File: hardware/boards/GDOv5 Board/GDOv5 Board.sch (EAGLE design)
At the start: 29 parts, among them IC1 DS1820, IC2 3.3V REG, J1 DCJ0202

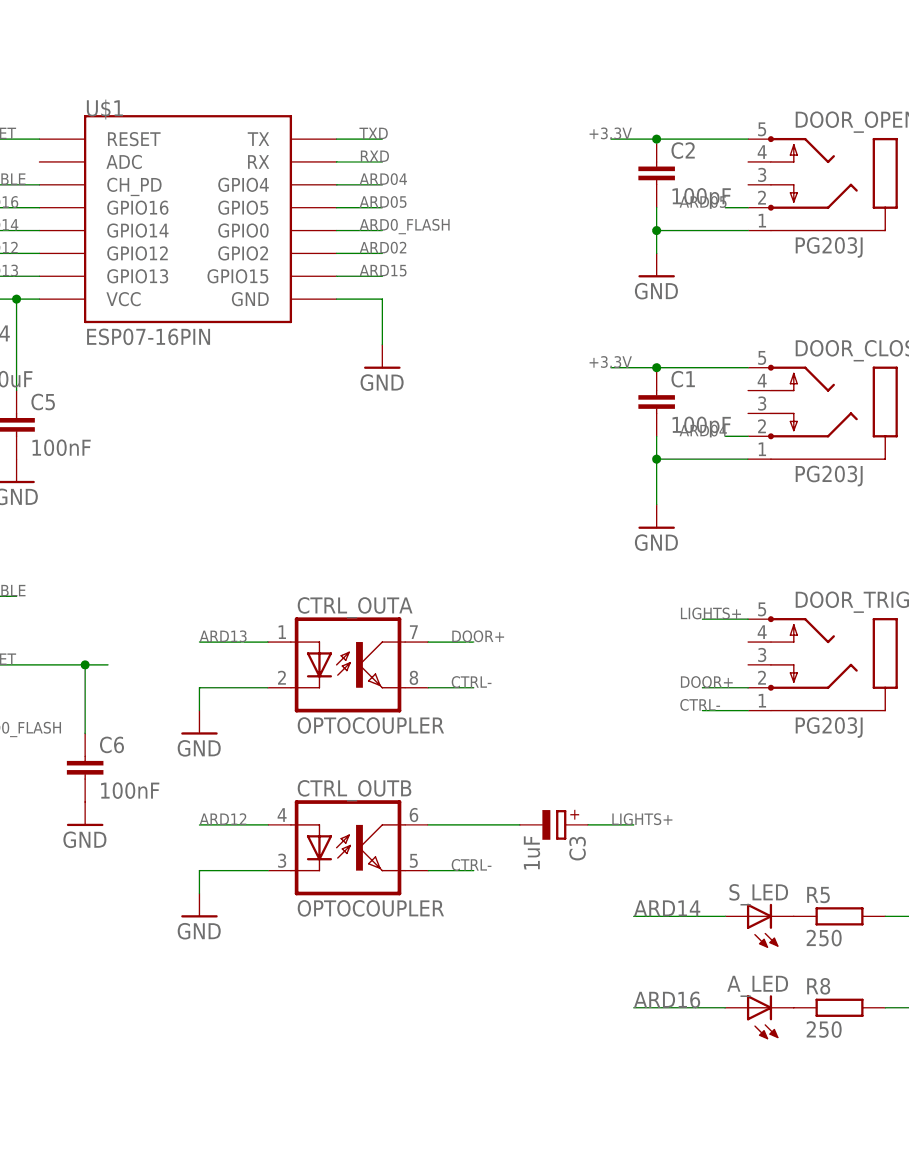
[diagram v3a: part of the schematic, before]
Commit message: Added resistor for optocoupler inputs
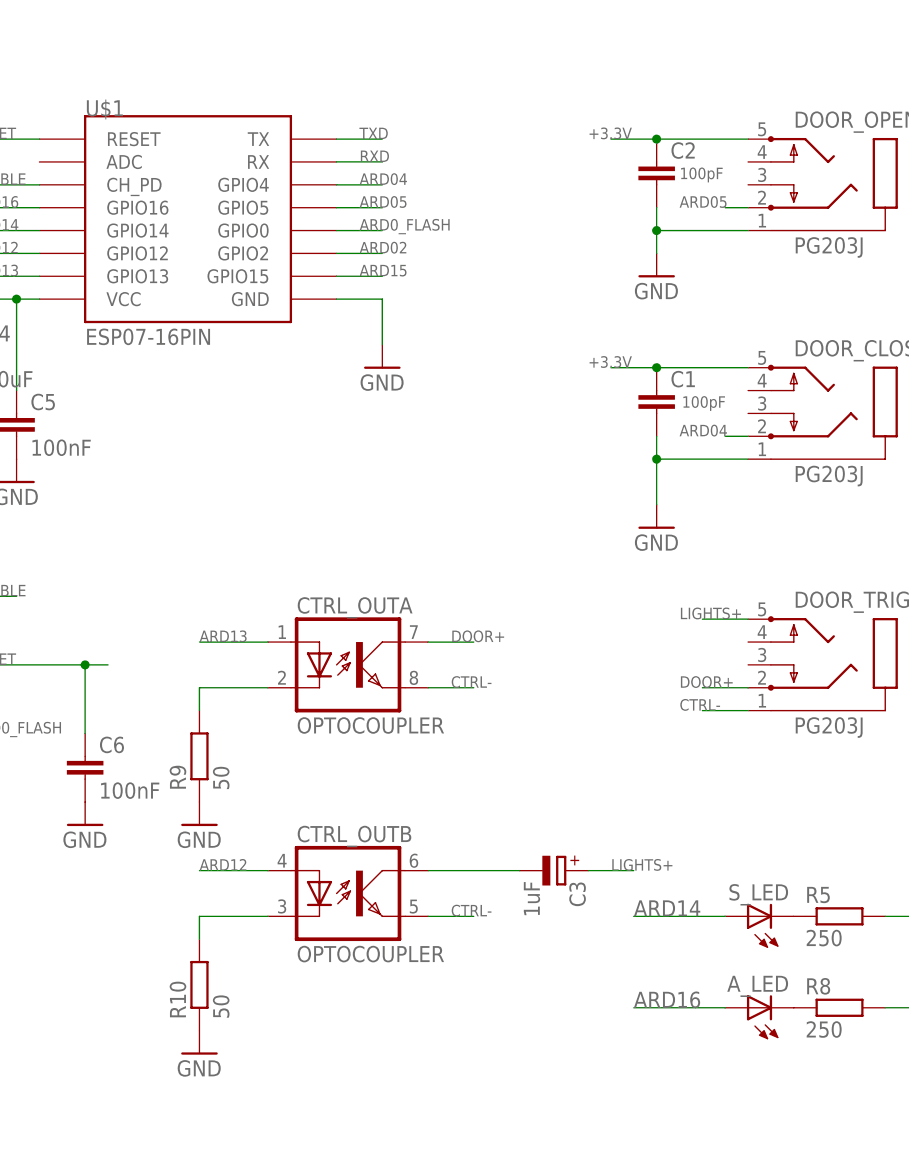
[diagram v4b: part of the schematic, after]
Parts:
- added R10, R9: 50, resistor:R-EU_M3216
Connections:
- new net N$6: CTRL_OUTA.C, R9.2
- new net N$7: CTRL_OUTB.C, R10.2
- net GND: now also R10.1, R9.1; no longer CTRL_OUTA.C, CTRL_OUTB.C
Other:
- moved on the sheet: C3, CTRL_OUTB
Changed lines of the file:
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@@
 <?xml version="1.0" encoding="utf-8"?>
 <!DOCTYPE eagle SYSTEM "eagle.dtd">
-<eagle version="7.5.0">
+<eagle version="7.4.0">
 <drawing>
 <settings>
@@
 <part name="C2" library="resistor" deviceset="C-EU" device="C1206" value="100pF"/>
 <part name="C3" library="rcl" deviceset="CPOL-EU" device="CT3216" value="1uF"/>
-<part name="GND5" library="supply1" deviceset="GND" device=""/>
-<part name="GND6" library="supply1" deviceset="GND" device=""/>
 <part name="GND7" library="supply1" deviceset="GND" device=""/>
 <part name="R1" library="resistor" deviceset="R-EU_" device="M3216" value="4.7K"/>
@@
 <part name="GND10" library="supply1" deviceset="GND" device=""/>
 <part name="GND12" library="supply1" deviceset="GND" device=""/>
+<part name="R9" library="resistor" deviceset="R-EU_" device="M3216" value="50"/>
+<part name="GND5" library="supply1" deviceset="GND" device=""/>
+<part name="R10" library="resistor" deviceset="R-EU_" device="M3216" value="50"/>
+<part name="GND13" library="supply1" deviceset="GND" device=""/>
 </parts>
 <sheets>
@@
 <instance part="J1" gate="G$1" x="-12.7" y="111.76"/>
 <instance part="CTRL_OUT" gate="A" x="93.98" y="40.64"/>
-<instance part="CTRL_OUT" gate="B" x="93.98" y="20.32"/>
+<instance part="CTRL_OUT" gate="B" x="93.98" y="15.24"/>
 <instance part="IC1" gate="G$1" x="-2.54" y="83.82"/>
 <instance part="IC2" gate="G$1" x="-5.08" y="53.34"/>
@@
 <instance part="GND3" gate="1" x="127" y="55.88"/>
 <instance part="GND4" gate="1" x="127" y="83.82"/>
-<instance part="C1" gate="G$1" x="127" y="71.12"/>
-<instance part="C2" gate="G$1" x="127" y="96.52"/>
-<instance part="C3" gate="G$1" x="116.84" y="22.86" rot="R270"/>
-<instance part="GND5" gate="1" x="76.2" y="33.02"/>
-<instance part="GND6" gate="1" x="76.2" y="12.7"/>
+<instance part="C1" gate="G$1" x="127" y="71.12" smashed="yes">
+<attribute name="NAME" x="128.524" y="71.501" size="1.778" layer="95"/>
+<attribute name="VALUE" x="129.794" y="69.215" size="1.27" layer="96"/>
+</instance>
+<instance part="C2" gate="G$1" x="127" y="96.52" smashed="yes">
+<attribute name="NAME" x="128.524" y="96.901" size="1.778" layer="95"/>
+<attribute name="VALUE" x="129.54" y="94.615" size="1.27" layer="96"/>
+</instance>
+<instance part="C3" gate="G$1" x="116.84" y="17.78" rot="R270"/>
 <instance part="GND7" gate="1" x="96.52" y="73.66"/>
 <instance part="R1" gate="G$1" x="-2.54" y="93.98"/>
@@
 <instance part="GND10" gate="1" x="157.48" y="-7.62"/>
 <instance part="GND12" gate="1" x="-2.54" y="71.12"/>
+<instance part="R9" gate="G$1" x="76.2" y="30.48" rot="R90"/>
+<instance part="GND5" gate="1" x="76.2" y="22.86"/>
+<instance part="R10" gate="G$1" x="76.2" y="5.08" rot="R90"/>
+<instance part="GND13" gate="1" x="76.2" y="-2.54"/>
 </instances>
 <busses>
@@
 </segment>
 <segment>
-<pinref part="CTRL_OUT" gate="A" pin="C"/>
-<wire x1="83.82" y1="38.1" x2="76.2" y2="38.1" width="0.1524" layer="91"/>
-<wire x1="76.2" y1="38.1" x2="76.2" y2="35.56" width="0.1524" layer="91"/>
-<pinref part="GND5" gate="1" pin="GND"/>
-</segment>
-<segment>
-<pinref part="CTRL_OUT" gate="B" pin="C"/>
-<wire x1="83.82" y1="17.78" x2="76.2" y2="17.78" width="0.1524" layer="91"/>
-<wire x1="76.2" y1="17.78" x2="76.2" y2="15.24" width="0.1524" layer="91"/>
-<pinref part="GND6" gate="1" pin="GND"/>
-</segment>
-<segment>
 <pinref part="U$1" gate="G$1" pin="GND"/>
 <wire x1="91.44" y1="81.28" x2="96.52" y2="81.28" width="0.1524" layer="91"/>
@@
 <wire x1="-2.54" y1="73.66" x2="-2.54" y2="71.12" width="0.1524" layer="91"/>
 <junction x="-2.54" y="73.66"/>
+</segment>
+<segment>
+<pinref part="R9" gate="G$1" pin="1"/>
+<pinref part="GND5" gate="1" pin="GND"/>
+</segment>
+<segment>
+<pinref part="R10" gate="G$1" pin="1"/>
+<pinref part="GND13" gate="1" pin="GND"/>
 </segment>
 </net>
@@
 <segment>
 <pinref part="CTRL_OUT" gate="B" pin="EMIT"/>
-<wire x1="101.6" y1="17.78" x2="106.68" y2="17.78" width="0.1524" layer="91"/>
-<label x="104.14" y="17.78" size="1.27" layer="95"/>
+<wire x1="101.6" y1="12.7" x2="106.68" y2="12.7" width="0.1524" layer="91"/>
+<label x="104.14" y="12.7" size="1.27" layer="95"/>
 </segment>
 <segment>
@@
 <segment>
 <pinref part="CTRL_OUT" gate="B" pin="COL"/>
-<wire x1="101.6" y1="22.86" x2="111.76" y2="22.86" width="0.1524" layer="91"/>
+<wire x1="101.6" y1="17.78" x2="111.76" y2="17.78" width="0.1524" layer="91"/>
 <pinref part="C3" gate="G$1" pin="-"/>
 </segment>
@@
 <segment>
 <pinref part="C3" gate="G$1" pin="+"/>
-<wire x1="119.38" y1="22.86" x2="124.46" y2="22.86" width="0.1524" layer="91"/>
-<label x="121.92" y="22.86" size="1.27" layer="95"/>
+<wire x1="119.38" y1="17.78" x2="124.46" y2="17.78" width="0.1524" layer="91"/>
+<label x="121.92" y="17.78" size="1.27" layer="95"/>
 </segment>
 <segment>
@@
 <segment>
 <pinref part="CTRL_OUT" gate="B" pin="A"/>
-<wire x1="83.82" y1="22.86" x2="76.2" y2="22.86" width="0.1524" layer="91"/>
-<label x="76.2" y="22.86" size="1.27" layer="95"/>
+<wire x1="83.82" y1="17.78" x2="76.2" y2="17.78" width="0.1524" layer="91"/>
+<label x="76.2" y="17.78" size="1.27" layer="95"/>
 </segment>
 <segment>
@@
 </segment>
 </net>
+<net name="N$6" class="0">
+<segment>
+<pinref part="CTRL_OUT" gate="A" pin="C"/>
+<wire x1="83.82" y1="38.1" x2="76.2" y2="38.1" width="0.1524" layer="91"/>
+<wire x1="76.2" y1="38.1" x2="76.2" y2="35.56" width="0.1524" layer="91"/>
+<pinref part="R9" gate="G$1" pin="2"/>
+</segment>
+</net>
+<net name="N$7" class="0">
+<segment>
+<pinref part="CTRL_OUT" gate="B" pin="C"/>
+<wire x1="83.82" y1="12.7" x2="76.2" y2="12.7" width="0.1524" layer="91"/>
+<wire x1="76.2" y1="12.7" x2="76.2" y2="10.16" width="0.1524" layer="91"/>
+<pinref part="R10" gate="G$1" pin="2"/>
+</segment>
+</net>

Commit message: More board tweaks
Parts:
- removed C5: 100nF, resistor:C-EUC1206
- added C8, C9: 10uF, SparkFun-Capacitors:10UF-TANT
- C3: device rcl:CPOL-EUCT3216 -> SparkFun-Capacitors:CAP1206
- C4: value 10uF -> 100nF
- D1, D2, D3: device diode:SCHOTTKY-DIODESMD -> adafruit:DIODESOD-123
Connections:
- net +3.3V: now also C9.+; no longer C5.1
- net +5V: now also C8.+
- net GND: now also C8.-, C9.-; no longer C5.2
- net LIGHTS+: now also C3.2; no longer C3.+
- net N$3: now also C3.1; no longer C3.-
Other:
- moved on the sheet: C4

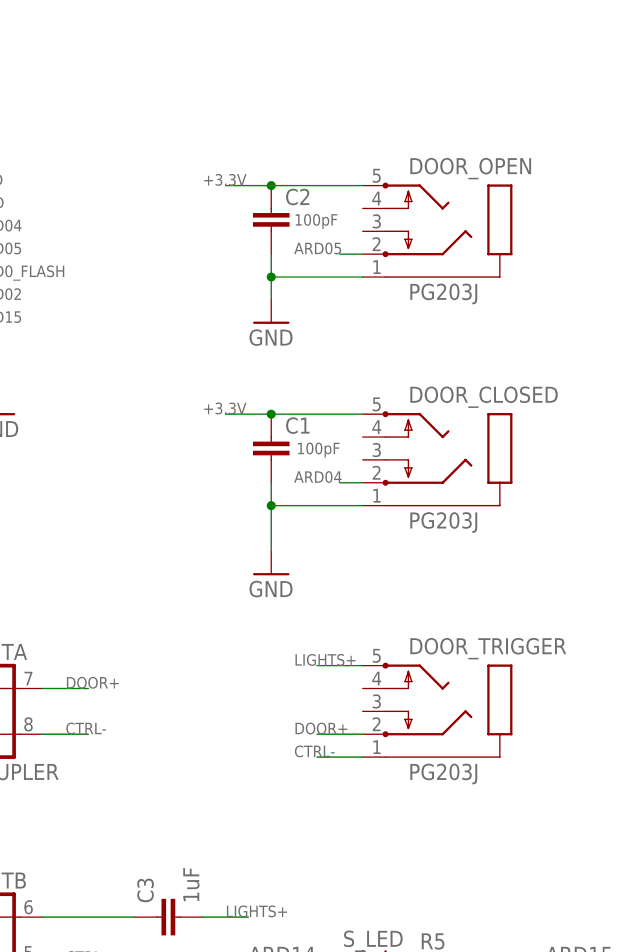
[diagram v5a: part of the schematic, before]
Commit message: Replacing 3.5mm Jack with SMT design
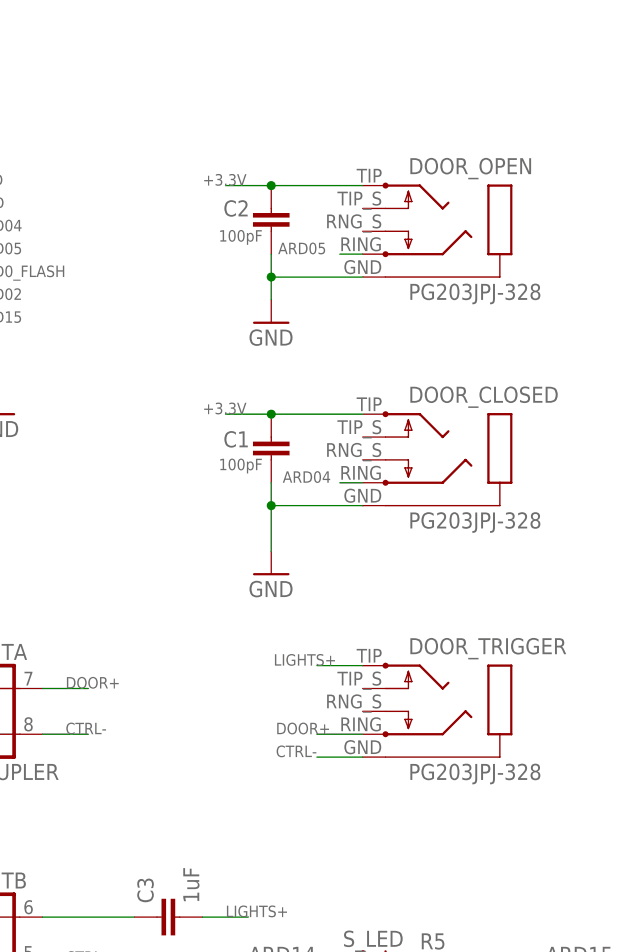
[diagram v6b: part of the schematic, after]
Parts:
- DOOR_CLOSED, DOOR_OPEN, DOOR_TRIGGER: value PG203J -> PG203JPJ-328; device con-hirschmann:PG203J -> PJ-328 Jack:PG203JPJ-328
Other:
- moved on the sheet: DOOR_CLOSED, DOOR_OPEN, DOOR_TRIGGER
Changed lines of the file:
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@@
 <grid distance="0.1" unitdist="inch" unit="inch" style="lines" multiple="1" display="no" altdistance="0.01" altunitdist="inch" altunit="inch"/>
 <layers>
-<layer number="1" name="Top" color="4" fill="1" visible="yes" active="no"/>
-<layer number="16" name="Bottom" color="1" fill="1" visible="yes" active="no"/>
-<layer number="17" name="Pads" color="2" fill="1" visible="yes" active="no"/>
-<layer number="18" name="Vias" color="2" fill="1" visible="yes" active="no"/>
-<layer number="19" name="Unrouted" color="6" fill="1" visible="yes" active="no"/>
-<layer number="20" name="Dimension" color="15" fill="1" visible="yes" active="no"/>
-<layer number="21" name="tPlace" color="7" fill="1" visible="yes" active="no"/>
-<layer number="22" name="bPlace" color="7" fill="1" visible="yes" active="no"/>
-<layer number="23" name="tOrigins" color="15" fill="1" visible="yes" active="no"/>
-<layer number="24" name="bOrigins" color="15" fill="1" visible="yes" active="no"/>
-<layer number="25" name="tNames" color="7" fill="1" visible="yes" active="no"/>
-<layer number="26" name="bNames" color="7" fill="1" visible="yes" active="no"/>
-<layer number="27" name="tValues" color="7" fill="1" visible="yes" active="no"/>
-<layer number="28" name="bValues" color="7" fill="1" visible="yes" active="no"/>
+<layer number="1" name="Top" color="4" fill="1" visible="no" active="no"/>
+<layer number="16" name="Bottom" color="1" fill="1" visible="no" active="no"/>
+<layer number="17" name="Pads" color="2" fill="1" visible="no" active="no"/>
+<layer number="18" name="Vias" color="2" fill="1" visible="no" active="no"/>
+<layer number="19" name="Unrouted" color="6" fill="1" visible="no" active="no"/>
+<layer number="20" name="Dimension" color="15" fill="1" visible="no" active="no"/>
+<layer number="21" name="tPlace" color="7" fill="1" visible="no" active="no"/>
+<layer number="22" name="bPlace" color="7" fill="1" visible="no" active="no"/>
+<layer number="23" name="tOrigins" color="15" fill="1" visible="no" active="no"/>
+<layer number="24" name="bOrigins" color="15" fill="1" visible="no" active="no"/>
+<layer number="25" name="tNames" color="7" fill="1" visible="no" active="no"/>
+<layer number="26" name="bNames" color="7" fill="1" visible="no" active="no"/>
+<layer number="27" name="tValues" color="7" fill="1" visible="no" active="no"/>
+<layer number="28" name="bValues" color="7" fill="1" visible="no" active="no"/>
 <layer number="29" name="tStop" color="7" fill="3" visible="no" active="no"/>
 <layer number="30" name="bStop" color="7" fill="6" visible="no" active="no"/>
@@
 <layer number="35" name="tGlue" color="7" fill="4" visible="no" active="no"/>
 <layer number="36" name="bGlue" color="7" fill="5" visible="no" active="no"/>
-<layer number="37" name="tTest" color="7" fill="1" visible="yes" active="no"/>
-<layer number="38" name="bTest" color="7" fill="1" visible="yes" active="no"/>
+<layer number="37" name="tTest" color="7" fill="1" visible="no" active="no"/>
+<layer number="38" name="bTest" color="7" fill="1" visible="no" active="no"/>
 <layer number="39" name="tKeepout" color="4" fill="11" visible="no" active="no"/>
 <layer number="40" name="bKeepout" color="1" fill="11" visible="no" active="no"/>
@@
 <layer number="44" name="Drills" color="7" fill="1" visible="no" active="no"/>
 <layer number="45" name="Holes" color="7" fill="1" visible="no" active="no"/>
-<layer number="46" name="Milling" color="3" fill="1" visible="yes" active="no"/>
-<layer number="47" name="Measures" color="7" fill="1" visible="yes" active="no"/>
-<layer number="48" name="Document" color="7" fill="1" visible="yes" active="no"/>
-<layer number="49" name="Reference" color="7" fill="1" visible="yes" active="no"/>
-<layer number="50" name="dxf" color="7" fill="1" visible="yes" active="no"/>
-<layer number="51" name="tDocu" color="7" fill="1" visible="yes" active="no"/>
-<layer number="52" name="bDocu" color="7" fill="1" visible="yes" active="no"/>
-<layer number="53" name="tGND_GNDA" color="7" fill="9" visible="yes" active="no"/>
-<layer number="54" name="bGND_GNDA" color="1" fill="9" visible="yes" active="no"/>
-<layer number="56" name="wert" color="7" fill="1" visible="yes" active="no"/>
-<layer number="57" name="tCAD" color="7" fill="1" visible="yes" active="no"/>
-<layer number="59" name="tCarbon" color="7" fill="1" visible="yes" active="no"/>
-<layer number="60" name="bCarbon" color="7" fill="1" visible="yes" active="no"/>
+<layer number="46" name="Milling" color="3" fill="1" visible="no" active="no"/>
+<layer number="47" name="Measures" color="7" fill="1" visible="no" active="no"/>
+<layer number="48" name="Document" color="7" fill="1" visible="no" active="no"/>
+<layer number="49" name="Reference" color="7" fill="1" visible="no" active="no"/>
+<layer number="50" name="dxf" color="7" fill="1" visible="no" active="no"/>
+<layer number="51" name="tDocu" color="7" fill="1" visible="no" active="no"/>
+<layer number="52" name="bDocu" color="7" fill="1" visible="no" active="no"/>
+<layer number="53" name="tGND_GNDA" color="7" fill="9" visible="no" active="no"/>
+<layer number="54" name="bGND_GNDA" color="1" fill="9" visible="no" active="no"/>
+<layer number="56" name="wert" color="7" fill="1" visible="no" active="no"/>
+<layer number="57" name="tCAD" color="7" fill="1" visible="no" active="no"/>
+<layer number="59" name="tCarbon" color="7" fill="1" visible="no" active="no"/>
+<layer number="60" name="bCarbon" color="7" fill="1" visible="no" active="no"/>
 <layer number="90" name="Modules" color="5" fill="1" visible="yes" active="yes"/>
 <layer number="91" name="Nets" color="2" fill="1" visible="yes" active="yes"/>
@@
 <parts>
 <part name="U$1" library="esp8266modules" deviceset="ESP07-16PIN" device=""/>
-<part name="DOOR_OPEN" library="con-hirschmann" deviceset="PG203J" device=""/>
-<part name="DOOR_CLOSED" library="con-hirschmann" deviceset="PG203J" device=""/>
-<part name="DOOR_TRIGGER" library="con-hirschmann" deviceset="PG203J" device=""/>
+<part name="DOOR_OPEN" library="PJ-328 Jack" deviceset="PG203J" device="PJ-328"/>
+<part name="DOOR_CLOSED" library="PJ-328 Jack" deviceset="PG203J" device="PJ-328"/>
+<part name="DOOR_TRIGGER" library="PJ-328 Jack" deviceset="PG203J" device="PJ-328"/>
 <part name="J1" library="con-jack" deviceset="DCJ0202" device=""/>
 <part name="CTRL_OUT" library="optocoupler" deviceset="ILD2" device="" value="OPTOCOUPLER"/>
@@
 <instance part="GND4" gate="1" x="127" y="83.82"/>
 <instance part="C1" gate="G$1" x="127" y="71.12" smashed="yes">
-<attribute name="NAME" x="128.524" y="71.501" size="1.778" layer="95"/>
-<attribute name="VALUE" x="129.794" y="69.215" size="1.27" layer="96"/>
+<attribute name="NAME" x="121.666" y="69.977" size="1.778" layer="95"/>
+<attribute name="VALUE" x="121.158" y="67.437" size="1.27" layer="96"/>
 </instance>
 <instance part="C2" gate="G$1" x="127" y="96.52" smashed="yes">
-<attribute name="NAME" x="128.524" y="96.901" size="1.778" layer="95"/>
-<attribute name="VALUE" x="129.54" y="94.615" size="1.27" layer="96"/>
+<attribute name="NAME" x="121.666" y="95.631" size="1.778" layer="95"/>
+<attribute name="VALUE" x="121.158" y="92.837" size="1.27" layer="96"/>
 </instance>
 <instance part="GND7" gate="1" x="96.52" y="73.66"/>
@@
 <pinref part="DOOR_OPEN" gate="1" pin="2"/>
 <wire x1="137.16" y1="91.44" x2="134.62" y2="91.44" width="0.1524" layer="91"/>
-<label x="129.54" y="91.44" size="1.27" layer="95"/>
+<label x="127.762" y="91.44" size="1.27" layer="95"/>
 </segment>
 <segment>
@@
 <pinref part="DOOR_CLOSED" gate="1" pin="2"/>
 <wire x1="137.16" y1="66.04" x2="134.62" y2="66.04" width="0.1524" layer="91"/>
-<label x="129.54" y="66.04" size="1.27" layer="95"/>
+<label x="128.27" y="66.04" size="1.27" layer="95"/>
 </segment>
 <segment>
@@
 <pinref part="DOOR_TRIGGER" gate="1" pin="2"/>
 <wire x1="137.16" y1="38.1" x2="132.08" y2="38.1" width="0.1524" layer="91"/>
-<label x="129.54" y="38.1" size="1.27" layer="95"/>
+<label x="127.508" y="38.1" size="1.27" layer="95"/>
 </segment>
 </net>
@@
 <pinref part="DOOR_TRIGGER" gate="1" pin="1"/>
 <wire x1="137.16" y1="35.56" x2="132.08" y2="35.56" width="0.1524" layer="91"/>
-<label x="129.54" y="35.56" size="1.27" layer="95"/>
+<label x="127.508" y="35.56" size="1.27" layer="95"/>
 </segment>
 </net>
@@
 <pinref part="DOOR_TRIGGER" gate="1" pin="5"/>
 <wire x1="137.16" y1="45.72" x2="132.08" y2="45.72" width="0.1524" layer="91"/>
-<label x="129.54" y="45.72" size="1.27" layer="95"/>
-</segment>
-</net>
+<label x="127.254" y="45.72" size="1.27" layer="95"/>
+</segment>
+</net>
